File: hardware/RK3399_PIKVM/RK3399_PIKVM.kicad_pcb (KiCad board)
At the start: 6 copper layers, 8 parts

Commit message: Made a testing design.
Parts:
- added ETH1: RJ45_Abracon_ARJP11A-MA_Horizontal, Connector_RJ:RJ45_Abracon_ARJP11A-MA_Horizontal, F.Cu at (90.0, 61.3)
- added ETH1 PHY: BGA80C65P10X10_700X700X100N, zgoolib:TC358870XBG, F.Cu at (104.0, 71.3)
- added ETH2: RJ45_Abracon_ARJP11A-MA_Horizontal, Connector_RJ:RJ45_Abracon_ARJP11A-MA_Horizontal, F.Cu at (90.0, 82.0)
- added ETH2 PHY: BGA80C65P10X10_700X700X100N, zgoolib:TC358870XBG, F.Cu at (104.0, 83.3)
- added GPIOs: PinHeader_2x15_P2.54mm_Vertical_SMD, Connector_PinHeader_2.54mm:PinHeader_2x15_P2.54mm_Vertical_SMD, F.Cu at (142.0, 144.8)
- added HDMI-IN: HDMI_A_Kycon_KDMIX-SL1-NS-WS-B15_VerticalRightAngle, Connector_HDMI:HDMI_A_Kycon_KDMIX-SL1-NS-WS-B15_VerticalRightAngle, F.Cu at (103.2, 140.5)
- added HDMI-OUT: HDMI_A_Kycon_KDMIX-SL1-NS-WS-B15_VerticalRightAngle, Connector_HDMI:HDMI_A_Kycon_KDMIX-SL1-NS-WS-B15_VerticalRightAngle, F.Cu at (115.0, 140.6)
- added M3: M3_Whole, zgoolib:M3_Whole, F.Cu at (74.0, 54.0)
- added M3: M3_Whole, zgoolib:M3_Whole, F.Cu at (166.0, 146.0)
- added M3: M3_Whole, zgoolib:M3_Whole, F.Cu at (166.0, 54.0)
- added M3: M3_Whole, zgoolib:M3_Whole, F.Cu at (74.0, 146.0)
- added Power_IN: DC-05_SMD, zgoolib:DC-05_SMD, F.Cu at (154.7, 59.5)
- added SD Card: TF-SMD_TF-02, zgoolib:TF-SMD_TF-02, F.Cu at (79.7, 108.0)
- added USB HUB: USB_A_Wuerth_61400826021_Horizontal_Stacked, Connector_USB:USB_A_Wuerth_61400826021_Horizontal_Stacked, F.Cu at (82.5, 134.1)
- added USB1: USB_C_Receptacle_HRO_TYPE-C-31-M-12, Connector_USB:USB_C_Receptacle_HRO_TYPE-C-31-M-12, F.Cu at (117.7, 54.3)
- added USB2: USB_C_Receptacle_HRO_TYPE-C-31-M-12, Connector_USB:USB_C_Receptacle_HRO_TYPE-C-31-M-12, F.Cu at (103.9, 54.2)
- moved RK808 22.5 mm to (130.7, 68.1)
- moved RAM 11.7 mm to (153.0, 111.8)
- moved RAM 11.7 mm to (143.7, 121.1)
- moved RAM 10.2 mm to (153.5, 88.0)
- moved RAM 10.2 mm to (144.3, 78.7)
- moved TC358870 7.52 mm to (103.7, 116.8)
- moved eMMC 6.67 mm to (103.7, 100.5)
- moved RK3399 6.15 mm to (130.4, 100.0)
- renumbered REF** to RAM, REF** to RK3399, REF** to RK808, REF** to TC358870, REF** to eMMC
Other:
- board outline added: 100 x 100 mm
- board text added: "QiKVM V1.0 Designed By Jeffrey"

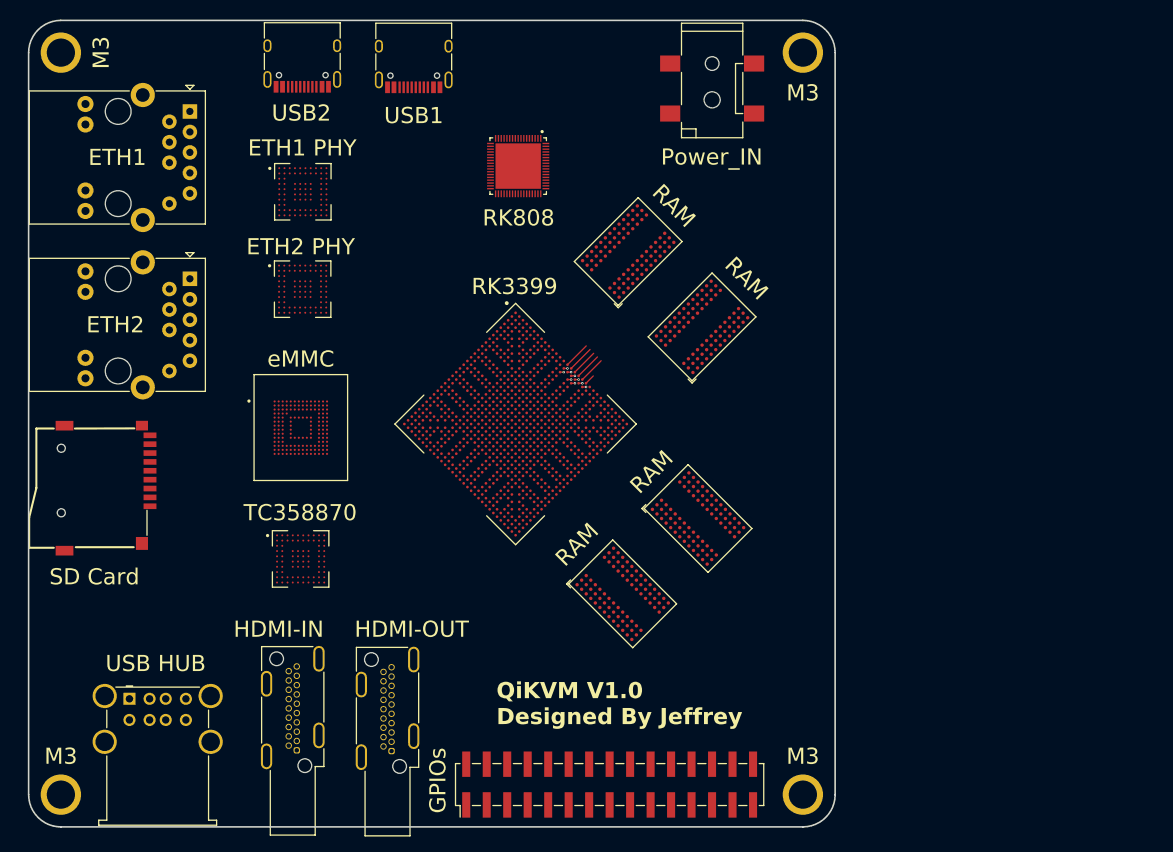
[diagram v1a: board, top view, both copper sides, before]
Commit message: Try to add PCIE-Mini port to the  board.
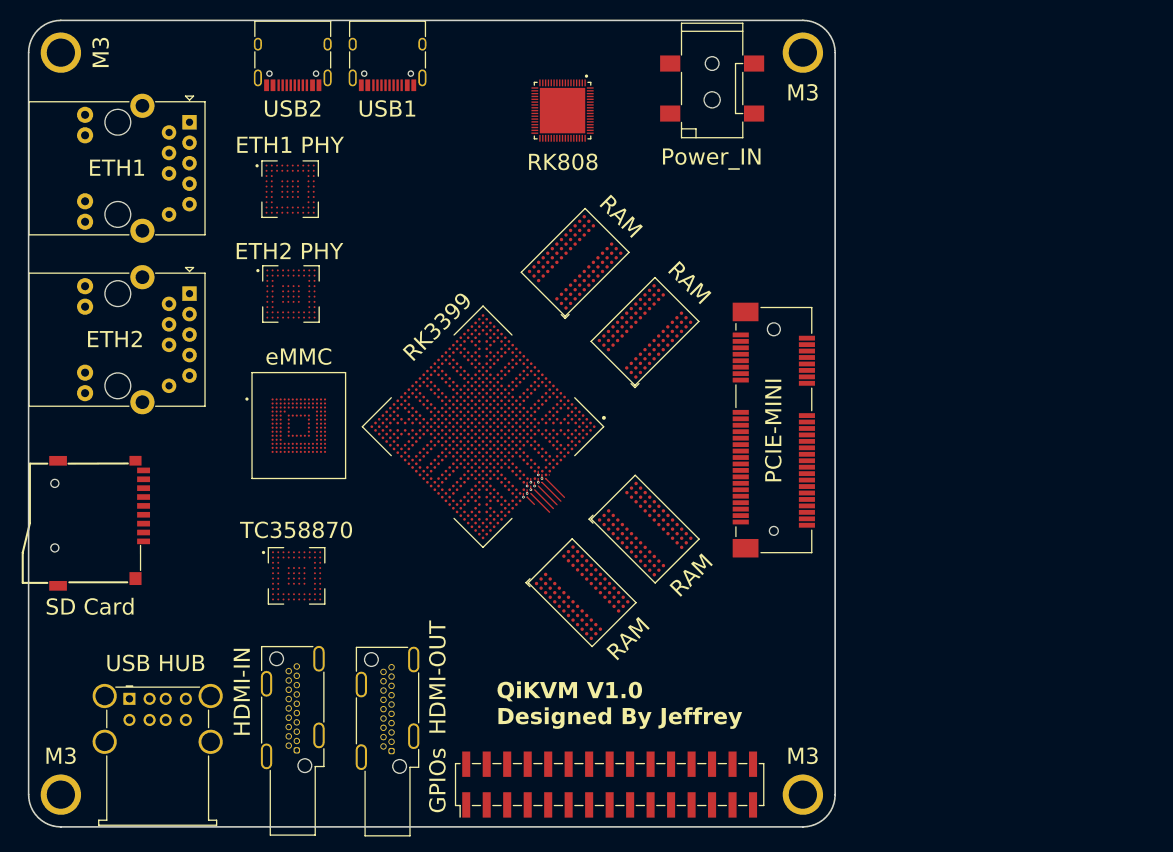
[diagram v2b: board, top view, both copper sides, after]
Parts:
- added PCIE-MINI: BUS_PCI_Express_Mini, Connector_PCBEdge:BUS_PCI_Express_Mini, F.Cu at (162.4, 100.8)
- moved RK808 8.81 mm to (136.2, 61.2)
- moved RAM 7.10 mm to (146.4, 88.6)
- moved RAM 6.71 mm to (137.8, 80.0)
- moved RAM 6.68 mm to (146.4, 113.1)
- moved RAM 5.03 mm to (138.6, 121.0)
- moved SD Card 4.43 mm to (78.9, 112.4)
- moved RK3399 4.05 mm to (126.3, 100.4), turned to -135 degrees
- moved USB1 3.26 mm to (114.5, 54.0)
- moved TC358870 2.16 mm to (103.2, 118.9)
- moved ETH2 1.84 mm to (89.9, 83.9)
- moved ETH1 PHY 1.61 mm to (102.4, 70.9)
- moved ETH2 PHY 1.57 mm to (102.5, 83.9)
- moved ETH1 1.34 mm to (89.9, 62.6)
- moved USB2 1.20 mm to (102.7, 54.0)
- moved eMMC 0.35 mm to (103.5, 100.3)

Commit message: Updated.
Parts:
- moved eMMC 1.25 mm to (102.2, 100.3)
- moved RK808 0.39 mm to (136.6, 61.1)
- moved USB HUB 0.25 mm to (82.7, 134.1)
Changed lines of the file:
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@@
   )
   (footprint "Connector_USB:USB_A_Wuerth_61400826021_Horizontal_Stacked" (layer "F.Cu")
-    (at 82.499999 134.120001)
+    (at 82.749999 134.120001)
     (descr "Stacked USB A connector http://katalog.we-online.de/em/datasheet/61400826021.pdf")
     (tags "Wuerth stacked USB_A")
@@
   )
   (footprint "zgoolib:FBGA-153" (layer "F.Cu")
-    (at 103.499999 100.250001)
+    (at 102.249999 100.250001)
     (attr smd)
-    (fp_text reference "eMMC" (at -0.000001 -8.499999) (layer "F.SilkS")
+    (fp_text reference "eMMC" (at -0.25 -8.5) (layer "F.SilkS")
         (effects (font (size 2 2) (thickness 0.2)))
     )
@@
   )
   (footprint "zgoolib:RK808D" (layer "F.Cu")
-    (at 136.199999 61.185001 -90)
+    (at 136.564999 61.050001 -90)
     (attr smd)
     (fp_text reference "RK808" (at 6.435 -0.05 -180) (layer "F.SilkS")

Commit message: Did little modification.
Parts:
- added REF**: PinHeader_2x05_P2.54mm_Vertical_SMD, Connector_PinHeader_2.54mm:PinHeader_2x05_P2.54mm_Vertical_SMD, F.Cu at (164.0, 127.6)
- moved PCIE-MINI 31.8 mm to (141.6, 76.7), turned to 0 degrees
- moved RAM 23.8 mm to (157.8, 93.0), turned to 90 degrees
- moved RAM 20.1 mm to (157.8, 105.2), turned to 90 degrees
- moved eMMC 12.8 mm to (115.0, 99.2)
- moved RAM 10.5 mm to (140.6, 121.8), turned to 0 degrees
- moved RAM 9.14 mm to (129.5, 121.8), turned to 0 degrees
- moved RK3399 8.96 mm to (135.2, 99.2), turned to 180 degrees
- moved ETH2 PHY 5.70 mm to (101.9, 89.6)
- moved ETH1 PHY 1.85 mm to (101.6, 69.3)
- moved RK808 1.41 mm to (137.6, 60.1)
- moved GPIOs 0.79 mm to (142.3, 144.0)
- moved TC358870 0.66 mm to (102.6, 118.8)

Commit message: Did some layout practice.
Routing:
- net (no net): track 34.5 -> 147.0 mm, vias 9 -> 2

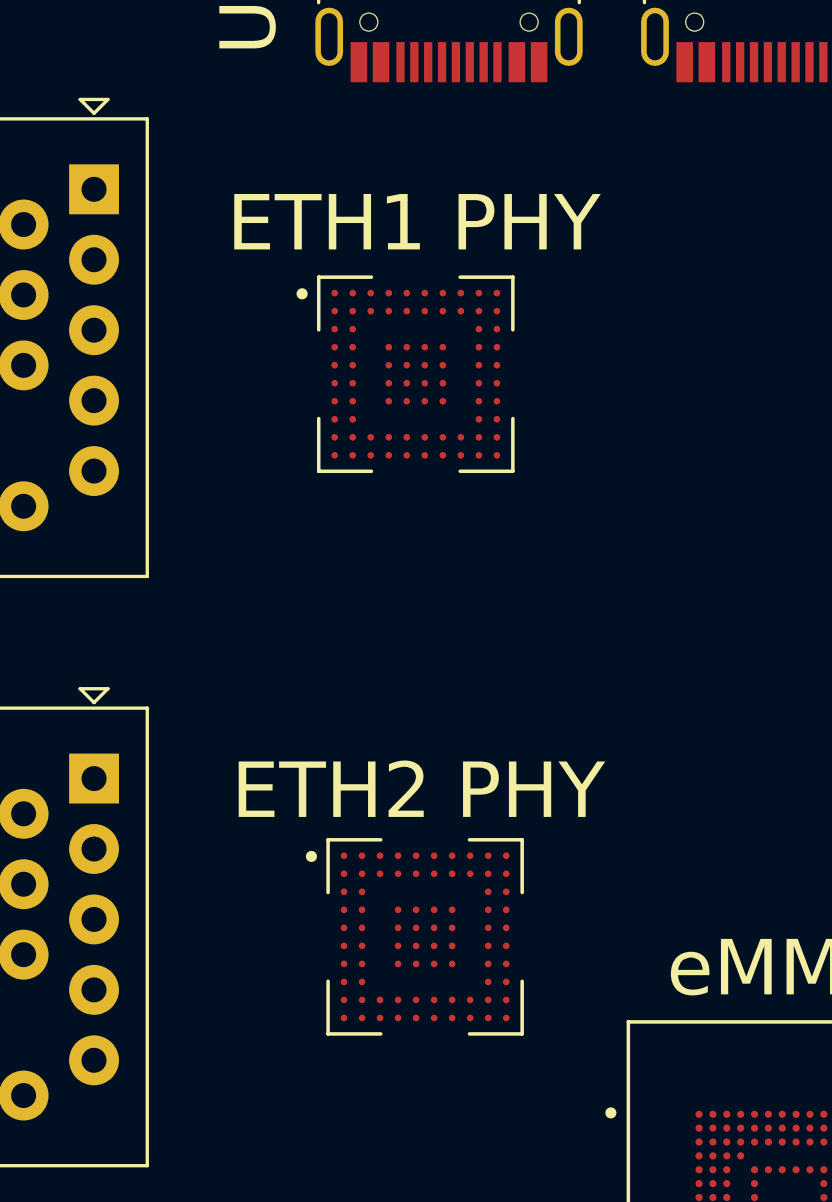
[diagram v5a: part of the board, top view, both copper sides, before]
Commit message: Use RTL8211 as the ETH PHY.
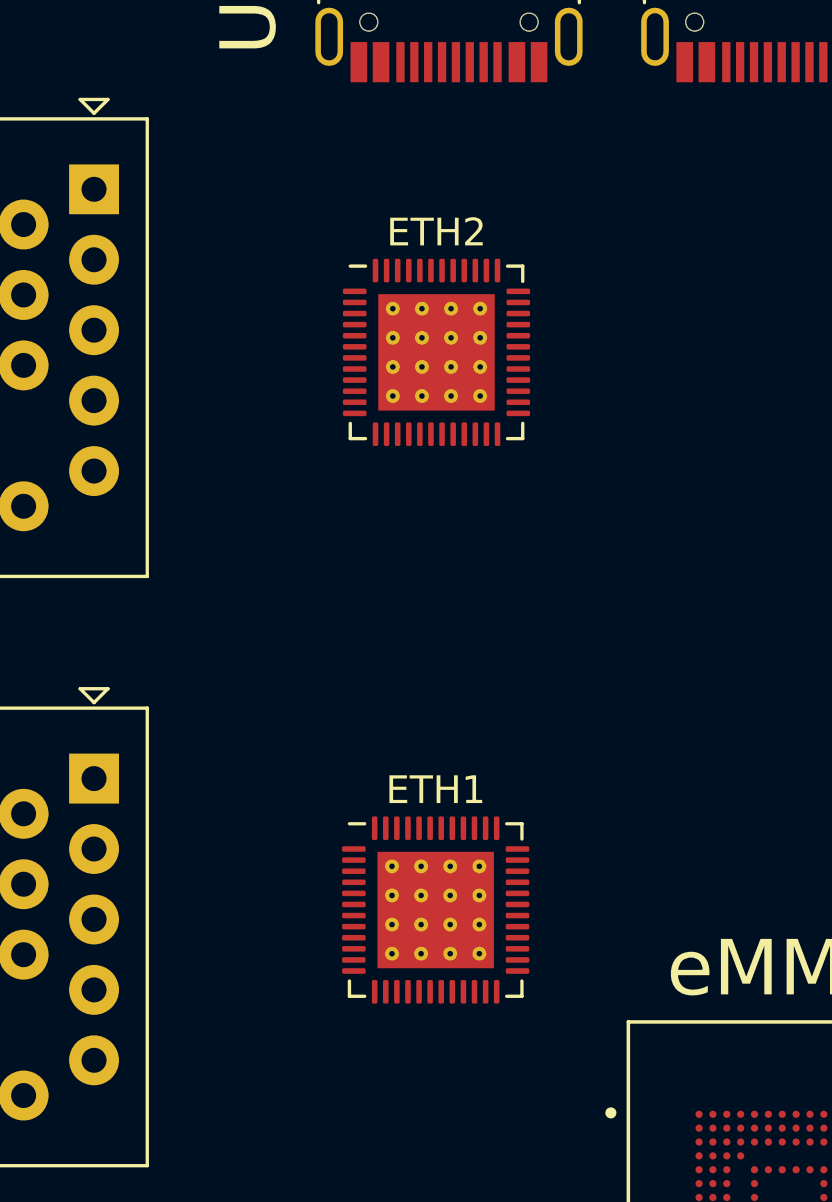
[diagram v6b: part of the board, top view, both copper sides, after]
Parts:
- removed ETH1 PHY: BGA80C65P10X10_700X700X100N, zgoolib:TC358870XBG
- removed ETH2 PHY: BGA80C65P10X10_700X700X100N, zgoolib:TC358870XBG
- added ETH1: QFN-48-1EP_6x6mm_P0.4mm_EP4.2x4.2mm_ThermalVias, Package_DFN_QFN:QFN-48-1EP_6x6mm_P0.4mm_EP4.2x4.2mm_ThermalVias, F.Cu at (102.3, 88.6)
- added ETH2: QFN-48-1EP_6x6mm_P0.4mm_EP4.2x4.2mm_ThermalVias, Package_DFN_QFN:QFN-48-1EP_6x6mm_P0.4mm_EP4.2x4.2mm_ThermalVias, F.Cu at (102.3, 68.5)

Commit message: Updated schematic
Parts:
- removed ETH1, ETH2: QFN-48-1EP_6x6mm_P0.4mm_EP4.2x4.2mm_ThermalVias, Package_DFN_QFN:QFN-48-1EP_6x6mm_P0.4mm_EP4.2x4.2mm_ThermalVias
- removed ETH1, ETH2: RJ45_Abracon_ARJP11A-MA_Horizontal, Connector_RJ:RJ45_Abracon_ARJP11A-MA_Horizontal
- removed GPIOs: PinHeader_2x15_P2.54mm_Vertical_SMD, Connector_PinHeader_2.54mm:PinHeader_2x15_P2.54mm_Vertical_SMD
- removed HDMI-IN, HDMI-OUT: HDMI_A_Kycon_KDMIX-SL1-NS-WS-B15_VerticalRightAngle, Connector_HDMI:HDMI_A_Kycon_KDMIX-SL1-NS-WS-B15_VerticalRightAngle
- removed PCIE-MINI: BUS_PCI_Express_Mini, Connector_PCBEdge:BUS_PCI_Express_Mini
- removed Power_IN: DC-05_SMD, zgoolib:DC-05_SMD
- removed RAM (x4): FBGA-78_7.5x11mm_Layout2x3x13_P0.8mm, Package_BGA:FBGA-78_7.5x11mm_Layout2x3x13_P0.8mm
- removed REF**: PinHeader_2x05_P2.54mm_Vertical_SMD, Connector_PinHeader_2.54mm:PinHeader_2x05_P2.54mm_Vertical_SMD
- removed RK3399: BGA828C65P31X31_2100X2100X161N, zgoolib:RK3399
- removed RK808: QFN35P700X700X80-69N, zgoolib:RK808D
- removed SD Card: TF-SMD_TF-02, zgoolib:TF-SMD_TF-02
- removed TC358870: BGA80C65P10X10_700X700X100N, zgoolib:TC358870XBG
- removed USB HUB: USB_A_Wuerth_61400826021_Horizontal_Stacked, Connector_USB:USB_A_Wuerth_61400826021_Horizontal_Stacked
- removed USB1, USB2: USB_C_Receptacle_HRO_TYPE-C-31-M-12, Connector_USB:USB_C_Receptacle_HRO_TYPE-C-31-M-12
- removed eMMC: BGA153C50P14X14_1150X1300X100N, zgoolib:FBGA-153
- added U1: RK3399, zgoolib:RK3399, F.Cu at (131.0, 92.4)
- added U2: ~, Package_BGA:BGA-96_9.0x13.0mm_Layout2x3x16_P0.8mm, F.Cu at (154.0, 98.5)
- added U3: ~, Package_BGA:BGA-96_9.0x13.0mm_Layout2x3x16_P0.8mm, F.Cu at (154.1, 86.6)
- added U4: ~, Package_BGA:BGA-96_9.0x13.0mm_Layout2x3x16_P0.8mm, F.Cu at (137.1, 113.5)
- added U5: ~, Package_BGA:BGA-96_9.0x13.0mm_Layout2x3x16_P0.8mm, F.Cu at (125.3, 113.5)
- added U6: ~, Package_DFN_QFN:QFN-68-1EP_8x8mm_P0.4mm_EP5.2x5.2mm, F.Cu at (124.3, 63.0)
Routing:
- net (no net): track 147.0 -> 0.00 mm, vias 2 -> 0

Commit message: Updated schematic
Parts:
- added J1: HR911105A, zgoolib:RJ45_HanRun_HR911105A, F.Cu at (87.3, 86.3)
- added J2: HR911105A, zgoolib:RJ45_HanRun_HR911105A, F.Cu at (87.3, 66.3)
- added U7: TPS54821RHLR, zgoolib:TPS54821, F.Cu at (129.0, 63.7)
- added U8: RTL8211F-CG, zgoolib:RTL8188_QFN40, F.Cu at (101.8, 91.1)
- added U9: RTL8111H-CG, Package_DFN_QFN:QFN-32-1EP_4x4mm_P0.4mm_EP2.65x2.65mm, F.Cu at (101.8, 72.7)
- moved U6 15.5 mm to (139.8, 62.0)
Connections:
- U1 pad A1: unconnected-(U1A-VSS_1-PadA1) -> VSS
- U1 pad A27: unconnected-(U1A-VSS_2-PadA27) -> VSS
- U1 pad A31: unconnected-(U1A-VSS_3-PadA31) -> VSS
- U1 pad AA10: unconnected-(U1A-VSS_179-PadAA10) -> VSS
- U1 pad AA11: unconnected-(U1B-AVSS_13-PadAA11) -> VSS
- U1 pad AA12: unconnected-(U1B-AVSS_17-PadAA12) -> VSS
- U1 pad AA13: unconnected-(U1A-VSS_177-PadAA13) -> VSS
- U1 pad AA14: unconnected-(U1B-AVSS_26-PadAA14) -> VSS
- U1 pad AA15: unconnected-(U1B-AVSS_53-PadAA15) -> VSS
- U1 pad AA19: Net-(U1K-NC-PadAA19) -> unconnected-(U1K-NC-PadAA19)
- U1 pad AA20: Net-(U1K-NC-PadAA19) -> unconnected-(U1K-NC-PadAA20)
- U1 pad AA22: Net-(U1K-NC-PadAA19) -> unconnected-(U1K-NC-PadAA22)
- U1 pad AA23: unconnected-(U1B-AVSS_4-PadAA23) -> VSS
- U1 pad AA26: unconnected-(U1B-AVSS_6-PadAA26) -> VSS
- U1 pad AA29: unconnected-(U1B-AVSS_7-PadAA29) -> VSS
- U1 pad AA3: unconnected-(U1A-VSS_4-PadAA3) -> VSS
- U1 pad AA5: unconnected-(U1A-VSS_5-PadAA5) -> VSS
- U1 pad AA9: unconnected-(U1A-VSS_6-PadAA9) -> VSS
- U1 pad AB10: unconnected-(U1B-AVSS_12-PadAB10) -> VSS
- U1 pad AB11: unconnected-(U1B-AVSS_8-PadAB11) -> VSS
- U1 pad AB13: unconnected-(U1B-AVSS_9-PadAB13) -> VSS
- U1 pad AB15: unconnected-(U1B-AVSS_42-PadAB15) -> VSS
- U1 pad AB16: unconnected-(U1B-AVSS_41-PadAB16) -> VSS
- U1 pad AB17: unconnected-(U1B-AVSS_52-PadAB17) -> VSS
- U1 pad AB19: unconnected-(U1A-VSS_140-PadAB19) -> VSS
- U1 pad AB20: Net-(U1K-NC-PadAA19) -> unconnected-(U1K-NC-PadAB20)
- U1 pad AB22: Net-(U1K-NC-PadAA19) -> unconnected-(U1K-NC-PadAB22)
- U1 pad AB23: unconnected-(U1B-AVSS_5-PadAB23) -> VSS
- U1 pad AB9: unconnected-(U1A-VSS_9-PadAB9) -> VSS
- U1 pad AC11: unconnected-(U1B-AVSS_44-PadAC11) -> VSS
- U1 pad AC12: Net-(U1K-NC-PadAA19) -> unconnected-(U1K-NC-PadAC12)
- U1 pad AC13: unconnected-(U1B-AVSS_45-PadAC13) -> VSS
- U1 pad AC14: Net-(U1K-NC-PadAA19) -> unconnected-(U1K-NC-PadAC14)
- U1 pad AC15: unconnected-(U1B-AVSS_10-PadAC15) -> VSS
- U1 pad AC16: unconnected-(U1B-AVSS_18-PadAC16) -> VSS
- U1 pad AC17: unconnected-(U1B-AVSS_43-PadAC17) -> VSS
- U1 pad AC18: unconnected-(U1A-VSS_145-PadAC18) -> VSS
- U1 pad AC20: unconnected-(U1A-VSS_13-PadAC20) -> VSS
- U1 pad AC21: unconnected-(U1A-VSS_132-PadAC21) -> VSS
- U1 pad AC22: unconnected-(U1A-VSS_12-PadAC22) -> VSS
- U1 pad AC23: unconnected-(U1B-AVSS_19-PadAC23) -> VSS
- U1 pad AC25: unconnected-(U1B-AVSS_51-PadAC25) -> VSS
- U1 pad AC26: unconnected-(U1B-AVSS_14-PadAC26) -> VSS
- U1 pad AC29: unconnected-(U1B-AVSS_15-PadAC29) -> VSS
- U1 pad AC3: unconnected-(U1A-VSS_16-PadAC3) -> VSS
- U1 pad AD10: unconnected-(U1A-VSS_19-PadAD10) -> VSS
- U1 pad AD11: Net-(U1K-NC-PadAA19) -> unconnected-(U1K-NC-PadAD11)
- U1 pad AD12: Net-(U1K-NC-PadAA19) -> unconnected-(U1K-NC-PadAD12)
- U1 pad AD13: unconnected-(U1B-AVSS_11-PadAD13) -> VSS
- U1 pad AD14: Net-(U1K-NC-PadAA19) -> unconnected-(U1K-NC-PadAD14)
- U1 pad AD15: Net-(U1K-NC-PadAA19) -> unconnected-(U1K-NC-PadAD15)
- U1 pad AD17: unconnected-(U1B-AVSS_16-PadAD17) -> VSS
- U1 pad AD21: unconnected-(U1A-VSS_163-PadAD21) -> VSS
- U1 pad AD22: unconnected-(U1A-VSS_11-PadAD22) -> VSS
- U1 pad AD26: unconnected-(U1B-AVSS_40-PadAD26) -> VSS
- U1 pad AD29: unconnected-(U1B-AVSS_20-PadAD29) -> VSS
- U1 pad AD3: unconnected-(U1A-VSS_17-PadAD3) -> VSS
- U1 pad AD5: unconnected-(U1A-VSS_18-PadAD5) -> VSS
- U1 pad AE11: unconnected-(U1B-AVSS_21-PadAE11) -> VSS
- U1 pad AE12: unconnected-(U1B-AVSS_22-PadAE12) -> VSS
- U1 pad AE14: unconnected-(U1B-AVSS_23-PadAE14) -> VSS
- U1 pad AE17: unconnected-(U1B-AVSS_24-PadAE17) -> VSS
- U1 pad AE23: unconnected-(U1A-VSS_14-PadAE23) -> VSS
- U1 pad AE27: unconnected-(U1B-AVSS_25-PadAE27) -> VSS
- U1 pad AF17: unconnected-(U1B-AVSS_27-PadAF17) -> VSS
- U1 pad AF18: unconnected-(U1A-VSS_7-PadAF18) -> VSS
- U1 pad AF20: unconnected-(U1A-VSS_10-PadAF20) -> VSS
- U1 pad AF23: unconnected-(U1B-AVSS_2-PadAF23) -> VSS
- U1 pad AF24: unconnected-(U1B-AVSS_3-PadAF24) -> VSS
- U1 pad AF29: unconnected-(U1B-AVSS_28-PadAF29) -> VSS
- U1 pad AF9: unconnected-(U1A-VSS_20-PadAF9) -> VSS
- U1 pad AG2: unconnected-(U1A-VSS_21-PadAG2) -> VSS
- U1 pad AG29: unconnected-(U1B-AVSS_29-PadAG29) -> VSS
- U1 pad AH29: unconnected-(U1B-AVSS_30-PadAH29) -> VSS
- U1 pad AJ11: unconnected-(U1B-AVSS_34-PadAJ11) -> VSS
- U1 pad AJ12: unconnected-(U1B-AVSS_35-PadAJ12) -> VSS
- U1 pad AJ14: unconnected-(U1B-AVSS_36-PadAJ14) -> VSS
- U1 pad AJ15: unconnected-(U1B-AVSS_37-PadAJ15) -> VSS
- U1 pad AJ17: unconnected-(U1B-AVSS_38-PadAJ17) -> VSS
- U1 pad AJ18: unconnected-(U1B-AVSS_39-PadAJ18) -> VSS
- U1 pad AJ20: unconnected-(U1A-VSS_180-PadAJ20) -> VSS
- U1 pad AJ21: unconnected-(U1A-VSS_172-PadAJ21) -> VSS
- U1 pad AJ23: unconnected-(U1A-VSS_173-PadAJ23) -> VSS
- U1 pad AJ24: unconnected-(U1A-VSS_174-PadAJ24) -> VSS
- U1 pad AJ26: unconnected-(U1A-VSS_175-PadAJ26) -> VSS
- U1 pad AJ27: unconnected-(U1A-VSS_176-PadAJ27) -> VSS
- U1 pad AJ28: unconnected-(U1A-VSS_171-PadAJ28) -> VSS
- U1 pad AJ29: unconnected-(U1B-AVSS_47-PadAJ29) -> VSS
- U1 pad AJ5: unconnected-(U1A-VSS_22-PadAJ5) -> VSS
- U1 pad AJ6: unconnected-(U1B-AVSS_31-PadAJ6) -> VSS
- U1 pad AJ8: unconnected-(U1B-AVSS_32-PadAJ8) -> VSS
- U1 pad AJ9: unconnected-(U1B-AVSS_33-PadAJ9) -> VSS
- U1 pad AL1: unconnected-(U1A-VSS_23-PadAL1) -> VSS
- U1 pad AL31: unconnected-(U1A-VSS_178-PadAL31) -> VSS
- U1 pad B5: unconnected-(U1A-VSS_24-PadB5) -> VSS
- U1 pad C11: unconnected-(U1A-VSS_27-PadC11) -> VSS
- U1 pad C12: unconnected-(U1A-VSS_28-PadC12) -> VSS
- U1 pad C14: unconnected-(U1A-VSS_29-PadC14) -> VSS
- U1 pad C15: unconnected-(U1A-VSS_30-PadC15) -> VSS
- U1 pad C17: unconnected-(U1A-VSS_31-PadC17) -> VSS
- U1 pad C18: unconnected-(U1A-VSS_32-PadC18) -> VSS
- U1 pad C20: unconnected-(U1A-VSS_33-PadC20) -> VSS
- U1 pad C21: unconnected-(U1A-VSS_34-PadC21) -> VSS
- U1 pad C23: unconnected-(U1A-VSS_35-PadC23) -> VSS
- U1 pad C24: unconnected-(U1A-VSS_36-PadC24) -> VSS
- U1 pad C26: unconnected-(U1A-VSS_37-PadC26) -> VSS
- U1 pad C8: unconnected-(U1A-VSS_25-PadC8) -> VSS
- U1 pad C9: unconnected-(U1A-VSS_26-PadC9) -> VSS
- U1 pad D5: unconnected-(U1A-VSS_38-PadD5) -> VSS
- U1 pad E12: unconnected-(U1A-VSS_42-PadE12) -> VSS
- U1 pad E15: unconnected-(U1A-VSS_43-PadE15) -> VSS
- U1 pad E18: unconnected-(U1A-VSS_44-PadE18) -> VSS
- U1 pad E2: unconnected-(U1A-VSS_39-PadE2) -> VSS
- U1 pad E21: unconnected-(U1A-VSS_45-PadE21) -> VSS
- U1 pad E24: unconnected-(U1A-VSS_46-PadE24) -> VSS
- U1 pad E31: unconnected-(U1A-VSS_47-PadE31) -> VSS
- U1 pad E4: unconnected-(U1A-VSS_40-PadE4) -> VSS
- U1 pad E7: unconnected-(U1A-VSS_41-PadE7) -> VSS
- U1 pad F15: unconnected-(U1A-VSS_49-PadF15) -> VSS
- U1 pad F18: unconnected-(U1A-VSS_50-PadF18) -> VSS
- U1 pad F20: unconnected-(U1A-VSS_51-PadF20) -> VSS
- U1 pad F21: unconnected-(U1A-VSS_52-PadF21) -> VSS
- U1 pad F8: unconnected-(U1A-VSS_48-PadF8) -> VSS
- U1 pad G18: unconnected-(U1A-VSS_55-PadG18) -> VSS
- U1 pad G27: unconnected-(U1A-VSS_56-PadG27) -> VSS
- U1 pad G5: unconnected-(U1A-VSS_53-PadG5) -> VSS
- U1 pad G9: unconnected-(U1A-VSS_54-PadG9) -> VSS
- U1 pad H10: unconnected-(U1A-VSS_59-PadH10) -> VSS
- U1 pad H11: unconnected-(U1A-VSS_60-PadH11) -> VSS
- U1 pad H12: unconnected-(U1A-VSS_61-PadH12) -> VSS
- U1 pad H13: unconnected-(U1A-VSS_62-PadH13) -> VSS
- U1 pad H15: unconnected-(U1A-VSS_63-PadH15) -> VSS
- U1 pad H16: unconnected-(U1A-VSS_64-PadH16) -> VSS
- U1 pad H17: unconnected-(U1A-VSS_65-PadH17) -> VSS
- U1 pad H18: unconnected-(U1A-VSS_66-PadH18) -> VSS
- U1 pad H26: unconnected-(U1A-VSS_67-PadH26) -> VSS
- U1 pad H3: unconnected-(U1A-VSS_57-PadH3) -> VSS
- U1 pad H9: unconnected-(U1A-VSS_58-PadH9) -> VSS
- U1 pad J10: unconnected-(U1A-VSS_73-PadJ10) -> VSS
- U1 pad J3: unconnected-(U1A-VSS_68-PadJ3) -> VSS
- U1 pad J6: unconnected-(U1A-VSS_69-PadJ6) -> VSS
- U1 pad J7: unconnected-(U1A-VSS_70-PadJ7) -> VSS
- U1 pad J8: unconnected-(U1A-VSS_71-PadJ8) -> VSS
- U1 pad J9: unconnected-(U1A-VSS_72-PadJ9) -> VSS
- U1 pad K10: unconnected-(U1A-VSS_76-PadK10) -> VSS
- U1 pad K12: unconnected-(U1A-VSS_77-PadK12) -> VSS
- U1 pad K14: unconnected-(U1A-VSS_78-PadK14) -> VSS
- U1 pad K16: unconnected-(U1A-VSS_79-PadK16) -> VSS
- U1 pad K18: unconnected-(U1A-VSS_80-PadK18) -> VSS
- U1 pad K20: unconnected-(U1A-VSS_82-PadK20) -> VSS
- U1 pad K22: unconnected-(U1A-VSS_84-PadK22) -> VSS
- U1 pad K8: unconnected-(U1A-VSS_74-PadK8) -> VSS
- U1 pad K9: unconnected-(U1A-VSS_75-PadK9) -> VSS
- U1 pad L11: unconnected-(U1A-VSS_88-PadL11) -> VSS
- U1 pad L12: unconnected-(U1A-VSS_89-PadL12) -> VSS
- U1 pad L13: unconnected-(U1A-VSS_90-PadL13) -> VSS
- U1 pad L14: unconnected-(U1A-VSS_91-PadL14) -> VSS
- U1 pad L15: unconnected-(U1A-VSS_92-PadL15) -> VSS
- U1 pad L16: unconnected-(U1A-VSS_93-PadL16) -> VSS
- U1 pad L20: unconnected-(U1A-VSS_96-PadL20) -> VSS
- U1 pad L22: unconnected-(U1A-VSS_97-PadL22) -> VSS
- U1 pad L27: unconnected-(U1A-VSS_99-PadL27) -> VSS
- U1 pad L3: unconnected-(U1A-VSS_85-PadL3) -> VSS
- U1 pad L6: unconnected-(U1A-VSS_86-PadL6) -> VSS
- U1 pad L8: unconnected-(U1A-VSS_87-PadL8) -> VSS
- U1 pad M10: unconnected-(U1A-VSS_102-PadM10) -> VSS
- U1 pad M16: unconnected-(U1A-VSS_103-PadM16) -> VSS
- U1 pad M23: unconnected-(U1A-VSS_104-PadM23) -> VSS
- U1 pad M3: unconnected-(U1A-VSS_100-PadM3) -> VSS
- U1 pad M8: unconnected-(U1A-VSS_101-PadM8) -> VSS
- U1 pad N13: unconnected-(U1A-VSS_108-PadN13) -> VSS
- U1 pad N14: unconnected-(U1A-VSS_109-PadN14) -> VSS
- U1 pad N15: unconnected-(U1A-VSS_110-PadN15) -> VSS
- U1 pad N16: unconnected-(U1A-VSS_111-PadN16) -> VSS
- U1 pad N17: unconnected-(U1A-VSS_94-PadN17) -> VSS
- U1 pad N19: unconnected-(U1A-VSS_83-PadN19) -> VSS
- U1 pad N21: unconnected-(U1A-VSS_98-PadN21) -> VSS
- U1 pad N8: unconnected-(U1A-VSS_105-PadN8) -> VSS
- U1 pad P10: unconnected-(U1A-VSS_116-PadP10) -> VSS
- U1 pad P11: unconnected-(U1A-VSS_106-PadP11) -> VSS
- U1 pad P12: unconnected-(U1A-VSS_107-PadP12) -> VSS
- U1 pad P16: unconnected-(U1A-VSS_117-PadP16) -> VSS
- U1 pad P19: unconnected-(U1A-VSS_119-PadP19) -> VSS
- U1 pad P21: unconnected-(U1A-VSS_121-PadP21) -> VSS
- U1 pad P3: unconnected-(U1A-VSS_112-PadP3) -> VSS
- U1 pad P6: unconnected-(U1A-VSS_113-PadP6) -> VSS
- U1 pad P7: unconnected-(U1A-VSS_114-PadP7) -> VSS
- U1 pad P8: unconnected-(U1A-VSS_115-PadP8) -> VSS
- U1 pad R14: unconnected-(U1A-VSS_129-PadR14) -> VSS
- U1 pad R15: unconnected-(U1A-VSS_130-PadR15) -> VSS
- U1 pad R16: unconnected-(U1A-VSS_131-PadR16) -> VSS
- U1 pad R18: unconnected-(U1A-VSS_165-PadR18) -> VSS
- U1 pad R21: unconnected-(U1A-VSS_120-PadR21) -> VSS
- U1 pad R23: unconnected-(U1A-VSS_133-PadR23) -> VSS
- U1 pad R3: unconnected-(U1A-VSS_123-PadR3) -> VSS
- U1 pad R5: unconnected-(U1A-VSS_124-PadR5) -> VSS
- U1 pad R6: unconnected-(U1A-VSS_125-PadR6) -> VSS
- U1 pad T10: unconnected-(U1A-VSS_135-PadT10) -> VSS
- U1 pad T16: unconnected-(U1A-VSS_138-PadT16) -> VSS
- U1 pad T18: unconnected-(U1A-VSS_168-PadT18) -> VSS
- U1 pad T19: unconnected-(U1A-VSS_122-PadT19) -> VSS
- U1 pad T21: unconnected-(U1A-VSS_139-PadT21) -> VSS
- U1 pad T8: unconnected-(U1A-VSS_134-PadT8) -> VSS
- U1 pad U11: unconnected-(U1A-VSS_126-PadU11) -> VSS
- U1 pad U12: unconnected-(U1A-VSS_127-PadU12) -> VSS
- U1 pad U14: unconnected-(U1A-VSS_137-PadU14) -> VSS
- U1 pad U15: unconnected-(U1A-VSS_143-PadU15) -> VSS
- U1 pad U16: unconnected-(U1A-VSS_144-PadU16) -> VSS
- U1 pad U19: unconnected-(U1A-VSS_146-PadU19) -> VSS
- U1 pad U21: unconnected-(U1A-VSS_147-PadU21) -> VSS
- U1 pad U22: unconnected-(U1A-VSS_149-PadU22) -> VSS
- U1 pad U23: unconnected-(U1B-AVSS_49-PadU23) -> VSS
- U1 pad U29: unconnected-(U1A-VSS_150-PadU29) -> VSS
- U1 pad U3: unconnected-(U1A-VSS_141-PadU3) -> VSS
- U1 pad U8: unconnected-(U1A-VSS_142-PadU8) -> VSS
- U1 pad V10: unconnected-(U1A-VSS_154-PadV10) -> VSS
- U1 pad V17: unconnected-(U1A-VSS_148-PadV17) -> VSS
- U1 pad V23: unconnected-(U1B-AVSS_50-PadV23) -> VSS
- U1 pad V3: unconnected-(U1A-VSS_151-PadV3) -> VSS
- U1 pad V5: unconnected-(U1A-VSS_152-PadV5) -> VSS
- U1 pad V8: unconnected-(U1A-VSS_153-PadV8) -> VSS
- U1 pad W13: unconnected-(U1A-VSS_128-PadW13) -> VSS
- U1 pad W17: unconnected-(U1A-VSS_159-PadW17) -> VSS
- U1 pad W18: unconnected-(U1A-VSS_169-PadW18) -> VSS
- U1 pad W19: unconnected-(U1A-VSS_167-PadW19) -> VSS
- U1 pad W21: unconnected-(U1A-VSS_81-PadW21) -> VSS
- U1 pad W22: unconnected-(U1A-VSS_158-PadW22) -> VSS
- U1 pad W23: unconnected-(U1B-AVSS_46-PadW23) -> VSS
- U1 pad W30: unconnected-(U1A-VSS_160-PadW30) -> VSS
- U1 pad W8: unconnected-(U1A-VSS_161-PadW8) -> VSS
- U1 pad W9: unconnected-(U1A-VSS_162-PadW9) -> VSS
- U1 pad Y10: unconnected-(U1A-VSS_15-PadY10) -> VSS
- U1 pad Y11: unconnected-(U1A-VSS_155-PadY11) -> VSS
- U1 pad Y12: unconnected-(U1A-VSS_136-PadY12) -> VSS
- U1 pad Y13: unconnected-(U1A-VSS_164-PadY13) -> VSS
- U1 pad Y14: unconnected-(U1A-VSS_156-PadY14) -> VSS
- U1 pad Y15: unconnected-(U1A-VSS_157-PadY15) -> VSS
- U1 pad Y16: unconnected-(U1A-VSS_118-PadY16) -> VSS
- U1 pad Y17: unconnected-(U1A-VSS_95-PadY17) -> VSS
- U1 pad Y20: unconnected-(U1A-VSS_170-PadY20) -> VSS
- U1 pad Y23: unconnected-(U1B-AVSS_1-PadY23) -> VSS
- U1 pad Y29: unconnected-(U1B-AVSS_48-PadY29) -> VSS
- U1 pad Y3: unconnected-(U1A-VSS_8-PadY3) -> VSS
- U1 pad Y9: unconnected-(U1A-VSS_166-PadY9) -> VSS
- U2 pad B2: unconnected-(U2-VDD#3-PadB2) -> Net-(U2-VDD#1)
- U2 pad D9: unconnected-(U2-VDD#7-PadD9) -> Net-(U2-VDD#1)
- U2 pad G7: unconnected-(U2-VDD#5-PadG7) -> Net-(U2-VDD#1)
- U2 pad K2: unconnected-(U2-VDD#4-PadK2) -> Net-(U2-VDD#1)
- U2 pad K8: unconnected-(U2-VDD#6-PadK8) -> Net-(U2-VDD#1)
- U2 pad N1: unconnected-(U2-VDD#1-PadN1) -> Net-(U2-VDD#1)
- U2 pad N9: unconnected-(U2-VDD#8-PadN9) -> Net-(U2-VDD#1)
- U2 pad R1: unconnected-(U2-VDD#2-PadR1) -> Net-(U2-VDD#1)
- U2 pad R9: unconnected-(U2-VDD#9-PadR9) -> Net-(U2-VDD#1)
- U3 pad B2: unconnected-(U3-VDD#3-PadB2) -> Net-(U3-VDD#1)
- U3 pad D9: unconnected-(U3-VDD#7-PadD9) -> Net-(U3-VDD#1)
- U3 pad G7: unconnected-(U3-VDD#5-PadG7) -> Net-(U3-VDD#1)
- U3 pad K2: unconnected-(U3-VDD#4-PadK2) -> Net-(U3-VDD#1)
- U3 pad K8: unconnected-(U3-VDD#6-PadK8) -> Net-(U3-VDD#1)
- U3 pad N1: unconnected-(U3-VDD#1-PadN1) -> Net-(U3-VDD#1)
- U3 pad N9: unconnected-(U3-VDD#8-PadN9) -> Net-(U3-VDD#1)
- U3 pad R1: unconnected-(U3-VDD#2-PadR1) -> Net-(U3-VDD#1)
- U3 pad R9: unconnected-(U3-VDD#9-PadR9) -> Net-(U3-VDD#1)
- U4 pad A1: unconnected-(U4-VDDQ#1-PadA1) -> Net-(U4-VDDQ#1)
- U4 pad A8: unconnected-(U4-VDDQ#6-PadA8) -> Net-(U4-VDDQ#1)
- U4 pad B2: unconnected-(U4-VDD#3-PadB2) -> Net-(U4-VDD#1)
- U4 pad C1: unconnected-(U4-VDDQ#2-PadC1) -> Net-(U4-VDDQ#1)
- U4 pad C9: unconnected-(U4-VDDQ#9-PadC9) -> Net-(U4-VDDQ#1)
- U4 pad D2: unconnected-(U4-VDDQ#4-PadD2) -> Net-(U4-VDDQ#1)
- U4 pad D9: unconnected-(U4-VDD#7-PadD9) -> Net-(U4-VDD#1)
- U4 pad E9: unconnected-(U4-VDDQ#8-PadE9) -> Net-(U4-VDDQ#1)
- U4 pad F1: unconnected-(U4-VDDQ#3-PadF1) -> Net-(U4-VDDQ#1)
- U4 pad G7: unconnected-(U4-VDD#5-PadG7) -> Net-(U4-VDD#1)
- U4 pad H2: unconnected-(U4-VDDQ#5-PadH2) -> Net-(U4-VDDQ#1)
- U4 pad H9: unconnected-(U4-VDDQ#7-PadH9) -> Net-(U4-VDDQ#1)
- U4 pad K2: unconnected-(U4-VDD#4-PadK2) -> Net-(U4-VDD#1)
- U4 pad K8: unconnected-(U4-VDD#6-PadK8) -> Net-(U4-VDD#1)
- U4 pad N1: unconnected-(U4-VDD#1-PadN1) -> Net-(U4-VDD#1)
- U4 pad N9: unconnected-(U4-VDD#8-PadN9) -> Net-(U4-VDD#1)
- U4 pad R1: unconnected-(U4-VDD#2-PadR1) -> Net-(U4-VDD#1)
- U4 pad R9: unconnected-(U4-VDD#9-PadR9) -> Net-(U4-VDD#1)
- U5 pad A1: unconnected-(U5-VDDQ#1-PadA1) -> Net-(U5-VDDQ#1)
- U5 pad A8: unconnected-(U5-VDDQ#6-PadA8) -> Net-(U5-VDDQ#1)
- U5 pad B2: unconnected-(U5-VDD#3-PadB2) -> Net-(U5-VDD#1)
- U5 pad C1: unconnected-(U5-VDDQ#2-PadC1) -> Net-(U5-VDDQ#1)
- U5 pad C9: unconnected-(U5-VDDQ#9-PadC9) -> Net-(U5-VDDQ#1)
- U5 pad D2: unconnected-(U5-VDDQ#4-PadD2) -> Net-(U5-VDDQ#1)
- U5 pad D9: unconnected-(U5-VDD#7-PadD9) -> Net-(U5-VDD#1)
- U5 pad E9: unconnected-(U5-VDDQ#8-PadE9) -> Net-(U5-VDDQ#1)
- U5 pad F1: unconnected-(U5-VDDQ#3-PadF1) -> Net-(U5-VDDQ#1)
- U5 pad G7: unconnected-(U5-VDD#5-PadG7) -> Net-(U5-VDD#1)
- U5 pad H2: unconnected-(U5-VDDQ#5-PadH2) -> Net-(U5-VDDQ#1)
- U5 pad H9: unconnected-(U5-VDDQ#7-PadH9) -> Net-(U5-VDDQ#1)
- U5 pad K2: unconnected-(U5-VDD#4-PadK2) -> Net-(U5-VDD#1)
- U5 pad K8: unconnected-(U5-VDD#6-PadK8) -> Net-(U5-VDD#1)
- U5 pad N1: unconnected-(U5-VDD#1-PadN1) -> Net-(U5-VDD#1)
- U5 pad N9: unconnected-(U5-VDD#8-PadN9) -> Net-(U5-VDD#1)
- U5 pad R1: unconnected-(U5-VDD#2-PadR1) -> Net-(U5-VDD#1)
- U5 pad R9: unconnected-(U5-VDD#9-PadR9) -> Net-(U5-VDD#1)
